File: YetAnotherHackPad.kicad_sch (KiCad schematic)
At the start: 11 parts, among them SW1 SW_Push, SW2 SW_Push, SW3 SW_Push, SW4 SW_Push, SW5 SW_Push, SW6 SW_Push, SW7 SW_Push, SW8 SW_Push, SW9 SW_Push, U1 XIAO-RP2040-DIP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

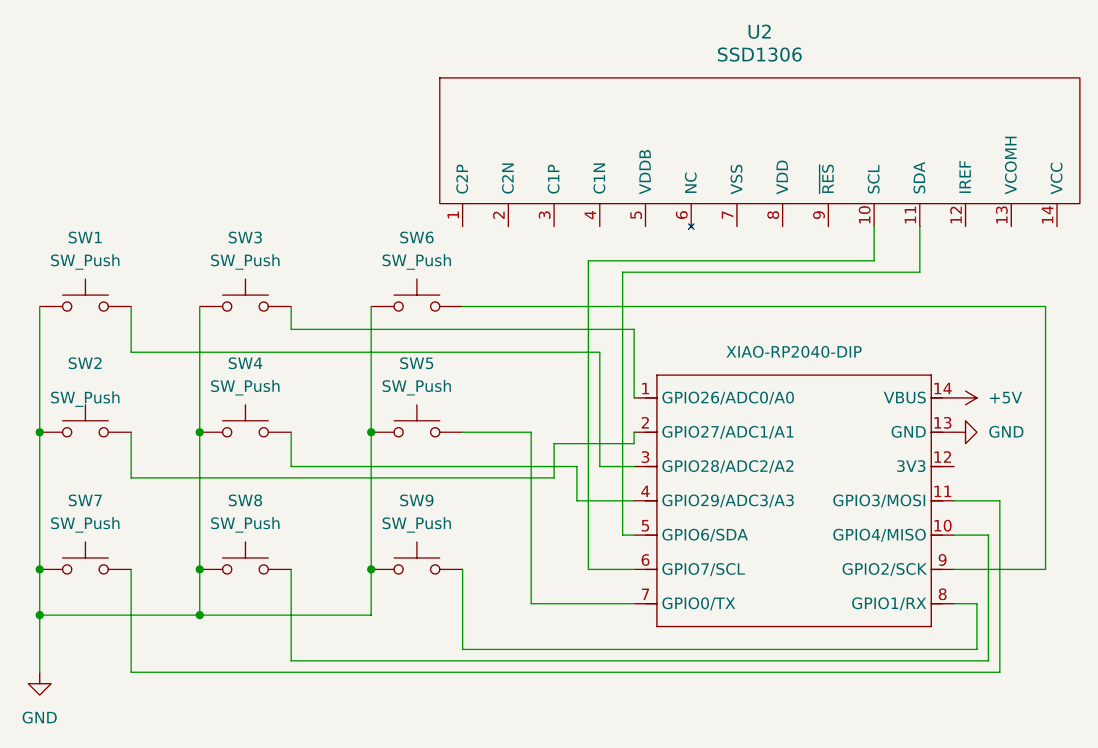
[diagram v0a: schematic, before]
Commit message: remove unneccesary diodes
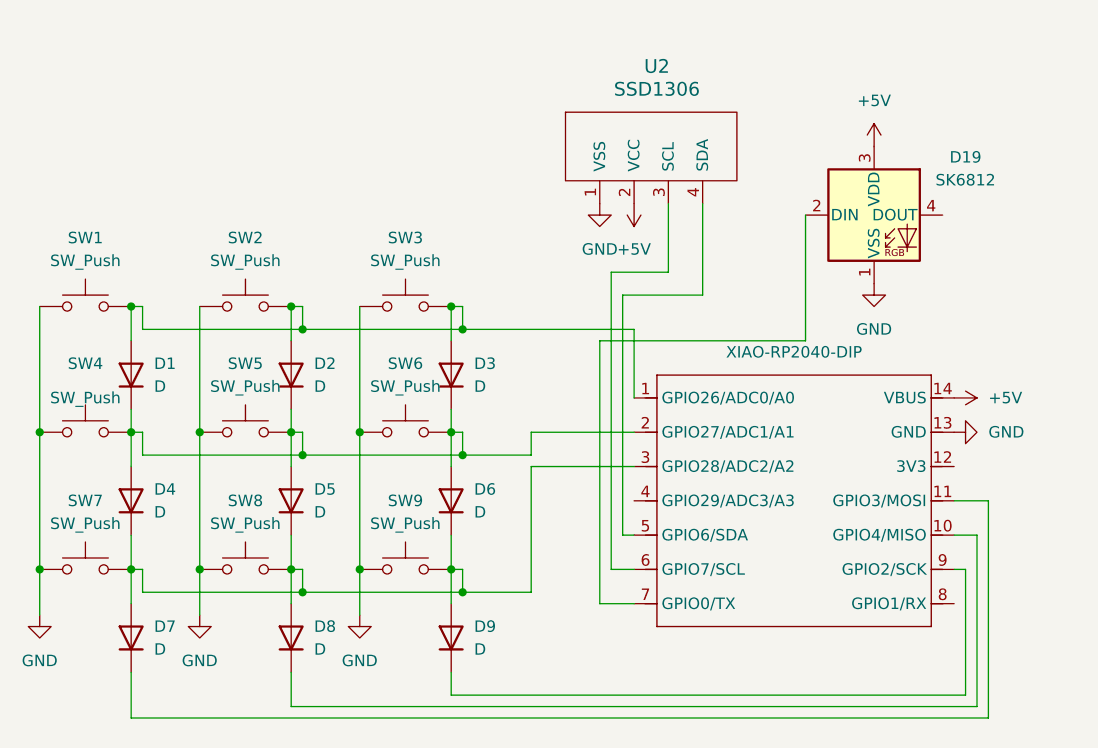
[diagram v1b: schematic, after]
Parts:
- added D1, D2, D3, D4, D5, D6, D7, D8, D9: D, Diode_THT:D_DO-35_SOD27_P7.62mm_Horizontal, symbol Device:D
- added D19: SK6812, LED_SMD:LED_SK6812_PLCC4_5.0x5.0mm_P3.2mm, symbol LED:SK6812
- U2: footprint SSD1306_OLED-0.91-128x32:SSD1306_OLED-0.91-128x32 -> KiCad-SSD1306-0.91-OLED-4pin-128x32:SSD1306-0.91-OLED-4pin-128x32
- renumbered SW3 to SW2, SW6 to SW3, SW2 to SW4, SW4 to SW5, SW5 to SW6
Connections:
- net +5V: now also U2.2 (VCC), D19.3 (VDD)
- net GND: now also U2.1 (VSS), D19.1 (VSS)
- net at SW7.2: now also SW8.2, SW9.2, U1.3 (GPIO28/ADC2/A2), D4.1 (K), D5.1 (K), D6.1 (K), D7.2 (A), D8.2 (A), D9.2 (A); no longer U1.11 (GPIO3/MOSI)
- net at SW4.2, U1.2 (GPIO27/ADC1/A1): now also SW5.2, SW6.2, D1.1 (K), D2.1 (K), D3.1 (K), D4.2 (A), D5.2 (A), D6.2 (A)
- net at SW2.2, U1.1 (GPIO26/ADC0/A0): now also SW1.2, SW3.2, D1.2 (A), D2.2 (A), D3.2 (A)
- net at U1.4 (GPIO29/ADC3/A3): no longer SW5.2
- net at U1.7 (GPIO0/TX): now also D19.2 (DIN); no longer SW6.2
- net at U1.10 (GPIO4/MISO): now also D8.1 (K); no longer SW8.2
- net at U1.6 (GPIO7/SCL): now also U2.3 (SCL); no longer U2.10 (SCL)
- net at U1.5 (GPIO6/SDA): now also U2.4 (SDA); no longer U2.11 (SDA)
- net at U1.8 (GPIO1/RX): no longer SW9.2
- net at U1.9 (GPIO2/SCK): now also D9.1 (K); no longer SW3.2
- new net: D7.1 (K), U1.11 (GPIO3/MOSI)
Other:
- moved on the sheet: SW3, SW6, SW9
